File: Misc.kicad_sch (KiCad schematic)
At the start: 18 parts, among them J1 BM04B-SURS-TFLFSN, J2 Conn_02x08_Top_Bottom, J3 Conn_01x04, J4 Conn_01x04, J5 Conn_01x05, J501 Conn_01x04, U2 SN65HVD232QDRQ1

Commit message: this is a message
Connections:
- net 17: now reaches J2.1 (Pin_1)
- net 38: now reaches J2.10 (Pin_10)
- net 38: now also J5.2 (Pin_2)
- net 37: now reaches J2.11 (Pin_11)
- net 37: now also J5.3 (Pin_3)
- net 36: now reaches J2.12 (Pin_12)
- net 36: now also J5.4 (Pin_4)
- net 35: now reaches J2.13 (Pin_13)
- net 35: now also J5.5 (Pin_5)
- net 34: now reaches J2.14 (Pin_14)
- net 34: now also J2.9 (Pin_9)
- net GPIO17: now reaches J2.15 (Pin_15)
- net GPIO17: now also J2.16 (Pin_16)
- net 20: now reaches J2.2 (Pin_2)
- net 21: now reaches J2.3 (Pin_3)
- net 22: now reaches J2.4 (Pin_4)
- net 23: now reaches J2.5 (Pin_5)
- net 24: now reaches J2.6 (Pin_6)
- net 25: now reaches J2.7 (Pin_7)
- net 26: now reaches J2.8 (Pin_8)
- net 39: now reaches J5.1 (Pin_1)
- net 43: now reaches J3.1 (Pin_1)
- net 42: now reaches J3.2 (Pin_2)
- net 41: now reaches J3.3 (Pin_3)
- net 40: now reaches J3.4 (Pin_4)
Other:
- moved on the sheet: J3
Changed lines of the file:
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@@
     (effects (font (size 0.4064 0.4064)) (justify left bottom))
   )
+  (global_label "37" (shape input) (at 52.07 82.55 0) (fields_autoplaced)
+    (effects (font (size 1.27 1.27)) (justify left))
+    (property "Intersheet References" "${INTERSHEET_REFS}" (id 0) (at 56.8132 82.4706 0)
+      (effects (font (size 1.27 1.27)) (justify left) hide)
+    )
+  )
+  (global_label "41" (shape input) (at 83.82 77.47 180) (fields_autoplaced)
+    (effects (font (size 1.27 1.27)) (justify right))
+    (property "Intersheet References" "${INTERSHEET_REFS}" (id 0) (at 79.0768 77.3906 0)
+      (effects (font (size 1.27 1.27)) (justify right) hide)
+    )
+  )
+  (global_label "36" (shape input) (at 52.07 85.09 0) (fields_autoplaced)
+    (effects (font (size 1.27 1.27)) (justify left))
+    (property "Intersheet References" "${INTERSHEET_REFS}" (id 0) (at 56.8132 85.0106 0)
+      (effects (font (size 1.27 1.27)) (justify left) hide)
+    )
+  )
+  (global_label "35" (shape input) (at 52.07 87.63 0) (fields_autoplaced)
+    (effects (font (size 1.27 1.27)) (justify left))
+    (property "Intersheet References" "${INTERSHEET_REFS}" (id 0) (at 56.8132 87.5506 0)
+      (effects (font (size 1.27 1.27)) (justify left) hide)
+    )
+  )
+  (global_label "39" (shape input) (at 73.66 107.95 180) (fields_autoplaced)
+    (effects (font (size 1.27 1.27)) (justify right))
+    (property "Intersheet References" "${INTERSHEET_REFS}" (id 0) (at 68.9168 108.0294 0)
+      (effects (font (size 1.27 1.27)) (justify right) hide)
+    )
+  )
+  (global_label "24" (shape input) (at 39.37 90.17 180) (fields_autoplaced)
+    (effects (font (size 1.27 1.27)) (justify right))
+    (property "Intersheet References" "${INTERSHEET_REFS}" (id 0) (at 34.6268 90.0906 0)
+      (effects (font (size 1.27 1.27)) (justify right) hide)
+    )
+  )
+  (global_label "GPIO17" (shape input) (at 52.07 92.71 0) (fields_autoplaced)
+    (effects (font (size 1.27 1.27)) (justify left))
+    (property "Intersheet References" "${INTERSHEET_REFS}" (id 0) (at 61.2885 92.7894 0)
+      (effects (font (size 1.27 1.27)) (justify left) hide)
+    )
+  )
+  (global_label "25" (shape input) (at 39.37 92.71 180) (fields_autoplaced)
+    (effects (font (size 1.27 1.27)) (justify right))
+    (property "Intersheet References" "${INTERSHEET_REFS}" (id 0) (at 34.6268 92.6306 0)
+      (effects (font (size 1.27 1.27)) (justify right) hide)
+    )
+  )
+  (global_label "34" (shape input) (at 52.07 90.17 0) (fields_autoplaced)
+    (effects (font (size 1.27 1.27)) (justify left))
+    (property "Intersheet References" "${INTERSHEET_REFS}" (id 0) (at 56.8132 90.0906 0)
+      (effects (font (size 1.27 1.27)) (justify left) hide)
+    )
+  )
+  (global_label "43" (shape input) (at 83.82 72.39 180) (fields_autoplaced)
+    (effects (font (size 1.27 1.27)) (justify right))
+    (property "Intersheet References" "${INTERSHEET_REFS}" (id 0) (at 79.0768 72.3106 0)
+      (effects (font (size 1.27 1.27)) (justify right) hide)
+    )
+  )
+  (global_label "17" (shape input) (at 39.37 77.47 180) (fields_autoplaced)
+    (effects (font (size 1.27 1.27)) (justify right))
+    (property "Intersheet References" "${INTERSHEET_REFS}" (id 0) (at 34.6268 77.3906 0)
+      (effects (font (size 1.27 1.27)) (justify right) hide)
+    )
+  )
+  (global_label "26" (shape input) (at 39.37 95.25 180) (fields_autoplaced)
+    (effects (font (size 1.27 1.27)) (justify right))
+    (property "Intersheet References" "${INTERSHEET_REFS}" (id 0) (at 34.6268 95.1706 0)
+      (effects (font (size 1.27 1.27)) (justify right) hide)
+    )
+  )
+  (global_label "22" (shape input) (at 39.37 85.09 180) (fields_autoplaced)
+    (effects (font (size 1.27 1.27)) (justify right))
+    (property "Intersheet References" "${INTERSHEET_REFS}" (id 0) (at 34.6268 85.0106 0)
+      (effects (font (size 1.27 1.27)) (justify right) hide)
+    )
+  )
+  (global_label "23" (shape input) (at 39.37 87.63 180) (fields_autoplaced)
+    (effects (font (size 1.27 1.27)) (justify right))
+    (property "Intersheet References" "${INTERSHEET_REFS}" (id 0) (at 34.6268 87.5506 0)
+      (effects (font (size 1.27 1.27)) (justify right) hide)
+    )
+  )
+  (global_label "21" (shape input) (at 39.37 82.55 180) (fields_autoplaced)
+    (effects (font (size 1.27 1.27)) (justify right))
+    (property "Intersheet References" "${INTERSHEET_REFS}" (id 0) (at 34.6268 82.4706 0)
+      (effects (font (size 1.27 1.27)) (justify right) hide)
+    )
+  )
+  (global_label "38" (shape input) (at 73.66 110.49 180) (fields_autoplaced)
+    (effects (font (size 1.27 1.27)) (justify right))
+    (property "Intersheet References" "${INTERSHEET_REFS}" (id 0) (at 68.9168 110.5694 0)
+      (effects (font (size 1.27 1.27)) (justify right) hide)
+    )
+  )
+  (global_label "40" (shape input) (at 83.82 80.01 180) (fields_autoplaced)
+    (effects (font (size 1.27 1.27)) (justify right))
+    (property "Intersheet References" "${INTERSHEET_REFS}" (id 0) (at 79.0768 79.9306 0)
+      (effects (font (size 1.27 1.27)) (justify right) hide)
+    )
+  )
   (global_label "MCU_CAN1_RX" (shape input) (at 149.86 46.99 180) (fields_autoplaced)
     (effects (font (size 1.27 1.27)) (justify right))
@@
     )
   )
+  (global_label "GPIO17" (shape input) (at 52.07 95.25 0) (fields_autoplaced)
+    (effects (font (size 1.27 1.27)) (justify left))
+    (property "Intersheet References" "${INTERSHEET_REFS}" (id 0) (at 61.2885 95.3294 0)
+      (effects (font (size 1.27 1.27)) (justify left) hide)
+    )
+  )
+  (global_label "34" (shape input) (at 52.07 77.47 0) (fields_autoplaced)
+    (effects (font (size 1.27 1.27)) (justify left))
+    (property "Intersheet References" "${INTERSHEET_REFS}" (id 0) (at 56.8132 77.3906 0)
+      (effects (font (size 1.27 1.27)) (justify left) hide)
+    )
+  )
+  (global_label "42" (shape input) (at 83.82 74.93 180) (fields_autoplaced)
+    (effects (font (size 1.27 1.27)) (justify right))
+    (property "Intersheet References" "${INTERSHEET_REFS}" (id 0) (at 79.0768 74.8506 0)
+      (effects (font (size 1.27 1.27)) (justify right) hide)
+    )
+  )
+  (global_label "36" (shape input) (at 73.66 115.57 180) (fields_autoplaced)
+    (effects (font (size 1.27 1.27)) (justify right))
+    (property "Intersheet References" "${INTERSHEET_REFS}" (id 0) (at 68.9168 115.6494 0)
+      (effects (font (size 1.27 1.27)) (justify right) hide)
+    )
+  )
+  (global_label "37" (shape input) (at 73.66 113.03 180) (fields_autoplaced)
+    (effects (font (size 1.27 1.27)) (justify right))
+    (property "Intersheet References" "${INTERSHEET_REFS}" (id 0) (at 68.9168 113.1094 0)
+      (effects (font (size 1.27 1.27)) (justify right) hide)
+    )
+  )
+  (global_label "35" (shape input) (at 73.66 118.11 180) (fields_autoplaced)
+    (effects (font (size 1.27 1.27)) (justify right))
+    (property "Intersheet References" "${INTERSHEET_REFS}" (id 0) (at 68.9168 118.1894 0)
+      (effects (font (size 1.27 1.27)) (justify right) hide)
+    )
+  )
+  (global_label "20" (shape input) (at 39.37 80.01 180) (fields_autoplaced)
+    (effects (font (size 1.27 1.27)) (justify right))
+    (property "Intersheet References" "${INTERSHEET_REFS}" (id 0) (at 34.6268 79.9306 0)
+      (effects (font (size 1.27 1.27)) (justify right) hide)
+    )
+  )
   (global_label "MCU_CAN1_TX" (shape input) (at 149.86 44.45 180) (fields_autoplaced)
     (effects (font (size 1.27 1.27)) (justify right))
     (property "Intersheet References" "${INTERSHEET_REFS}" (id 0) (at 40.64 -91.44 0)
       (effects (font (size 1.27 1.27)) hide)
+    )
+  )
+  (global_label "38" (shape input) (at 52.07 80.01 0) (fields_autoplaced)
+    (effects (font (size 1.27 1.27)) (justify left))
+    (property "Intersheet References" "${INTERSHEET_REFS}" (id 0) (at 56.8132 79.9306 0)
+      (effects (font (size 1.27 1.27)) (justify left) hide)
     )
   )
@@
     (pin "1")
   )
-  (symbol (lib_id "Connector_Generic:Conn_01x04") (at 78.74 78.74 0) (unit 1)
+  (symbol (lib_id "Connector_Generic:Conn_01x04") (at 88.9 74.93 0) (unit 1)
     (in_bom yes) (on_board yes) (fields_autoplaced)
-    (property "Reference" "J3" (id 0) (at 81.28 78.7399 0)
-      (effects (font (size 1.27 1.27)) (justify left))
-    )
-    (property "Value" "Conn_01x04" (id 1) (at 81.28 81.2799 0)
-      (effects (font (size 1.27 1.27)) (justify left))
-    )
-    (property "Footprint" "Connector_PinSocket_2.54mm:PinSocket_1x04_P2.54mm_Vertical" (id 2) (at 78.74 78.74 0)
-      (effects (font (size 1.27 1.27)) hide)
-    )
-    (property "Datasheet" "~" (id 3) (at 78.74 78.74 0)
-      (effects (font (size 1.27 1.27)) hide)
-    )
+    (property "Reference" "J3" (id 0) (at 91.44 74.9299 0)
+      (effects (font (size 1.27 1.27)) (justify left))
+    )
+    (property "Value" "Conn_01x04" (id 1) (at 91.44 77.4699 0)
+      (effects (font (size 1.27 1.27)) (justify left))
+    )
+    (property "Footprint" "Connector_PinSocket_2.54mm:PinSocket_1x04_P2.54mm_Vertical" (id 2) (at 88.9 74.93 0)
+      (effects (font (size 1.27 1.27)) hide)
+    )
+    (property "Datasheet" "~" (id 3) (at 88.9 74.93 0)
+      (effects (font (size 1.27 1.27)) hide)
+    )

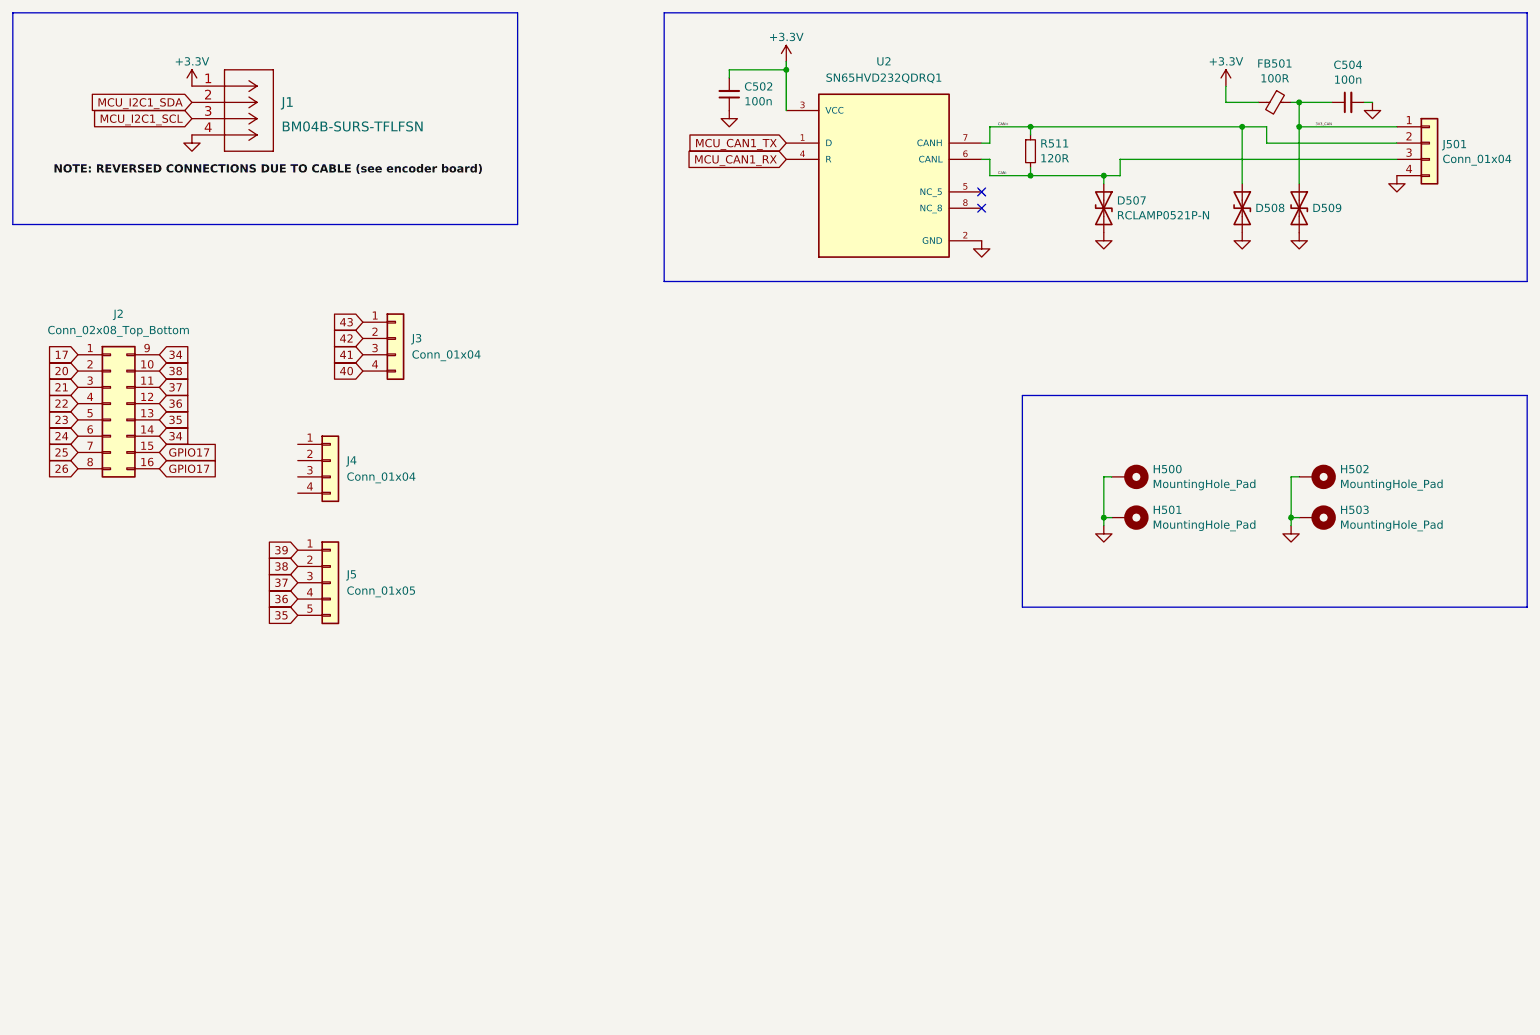
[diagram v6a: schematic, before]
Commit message: gpio breakout stuff
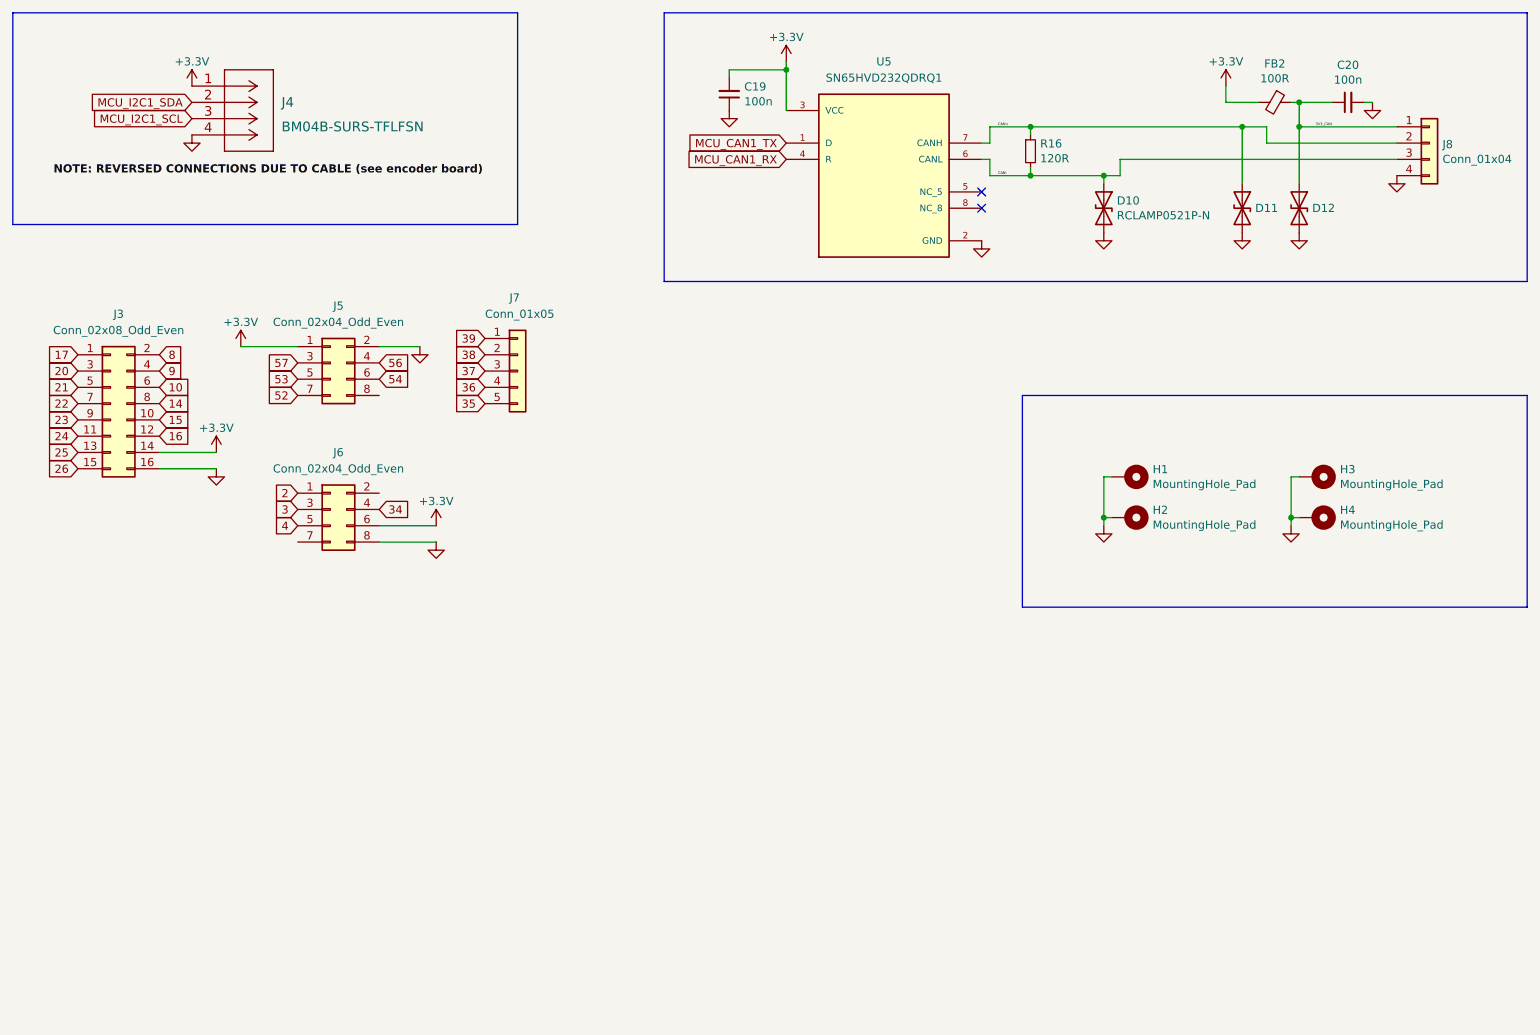
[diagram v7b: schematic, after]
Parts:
- removed J2: Conn_02x08_Top_Bottom, Connector_PinSocket_2.54mm:PinSocket_2x08_P2.54mm_Vertical, symbol Connector_Generic:Conn_02x08_Top_Bottom
- removed J3, J4: Conn_01x04, Connector_PinSocket_2.54mm:PinSocket_1x04_P2.54mm_Vertical, symbol Connector_Generic:Conn_01x04
- added J3: Conn_02x08_Odd_Even, Connector_PinHeader_2.54mm:PinHeader_2x08_P2.54mm_Vertical, symbol Connector_Generic:Conn_02x08_Odd_Even
- added J5, J6: Conn_02x04_Odd_Even, Connector_PinHeader_2.54mm:PinHeader_2x04_P2.54mm_Vertical, symbol Connector_Generic:Conn_02x04_Odd_Even
- renumbered C502 to C19, C504 to C20, D507 to D10, D508 to D11, D509 to D12, FB501 to FB2, H500 to H1, H501 to H2, H502 to H3, H503 to H4, J1 to J4, J5 to J7, J501 to J8, R511 to R16, U2 to U5
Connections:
- net +3V3: now also J3.14 (Pin_14), J5.1 (Pin_1), J6.6 (Pin_6)
- net 17: now also J3.1 (Pin_1)
- net 20: now also J3.3 (Pin_3)
- net 21: now also J3.5 (Pin_5)
- net 22: now also J3.7 (Pin_7)
- net 23: now also J3.9 (Pin_9)
- net 24: now also J3.11 (Pin_11)
- net 25: now also J3.13 (Pin_13)
- net 26: now also J3.15 (Pin_15)
- net 34: now also J6.4 (Pin_4)
- net GND: now also J3.16 (Pin_16), J5.2 (Pin_2), J6.8 (Pin_8)
- new net 10: J3.6 (Pin_6)
- new net 14: J3.8 (Pin_8)
- new net 15: J3.10 (Pin_10)
- new net 16: J3.12 (Pin_12)
- new net 2: J6.1 (Pin_1)
- new net 3: J6.3 (Pin_3)
- new net 4: J6.5 (Pin_5)
- new net 52: J5.7 (Pin_7)
- new net 53: J5.5 (Pin_5)
- new net 54: J5.6 (Pin_6)
- new net 56: J5.4 (Pin_4)
- new net 57: J5.3 (Pin_3)
- new net 8: J3.2 (Pin_2)
- new net 9: J3.4 (Pin_4)
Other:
- moved on the sheet: J7

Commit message: stuff
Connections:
- net 34 is gone; now on net 10: J6.4 (Pin_4)
- net +3V3: now also J6.1 (Pin_1); no longer J3.14 (Pin_14), J6.6 (Pin_6)
- net 10: no longer J3.6 (Pin_6)
- net 17: no longer J3.1 (Pin_1)
- net 2: now also J6.7 (Pin_7); no longer J6.1 (Pin_1)
- net 20: no longer J3.3 (Pin_3)
- net 21: no longer J3.5 (Pin_5)
- net 22: no longer J3.7 (Pin_7)
- net 23: no longer J3.9 (Pin_9)
- net 24: no longer J3.11 (Pin_11)
- net 25: no longer J3.13 (Pin_13)
- net 26: no longer J3.15 (Pin_15)
- net 3: now also J6.5 (Pin_5); no longer J6.3 (Pin_3)
- net 4: now also J6.3 (Pin_3); no longer J6.5 (Pin_5)
- net 52: now also J5.6 (Pin_6); no longer J5.7 (Pin_7)
- net 53: now also J5.8 (Pin_8); no longer J5.5 (Pin_5)
- net 54: now also J5.3 (Pin_3); no longer J5.6 (Pin_6)
- net 56: now also J5.5 (Pin_5); no longer J5.4 (Pin_4)
- net 57: now also J5.7 (Pin_7); no longer J5.3 (Pin_3)
- net 8: now also J6.8 (Pin_8); no longer J3.2 (Pin_2)
- net 9: now also J6.6 (Pin_6); no longer J3.4 (Pin_4)
- net GND: now also J3.2 (Pin_2), J6.2 (Pin_2); no longer J3.16 (Pin_16), J6.8 (Pin_8)
- net 35 renamed 43
- net 36 renamed 42
- net 37 renamed 41
- net 38 renamed 40
- new net +5V: J3.1 (Pin_1)
- new net 50: J5.4 (Pin_4)
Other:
- moved on the sheet: J3, J5, J6, J7
